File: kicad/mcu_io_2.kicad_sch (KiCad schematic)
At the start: 1 part, among them U5 MCXN947VDFT

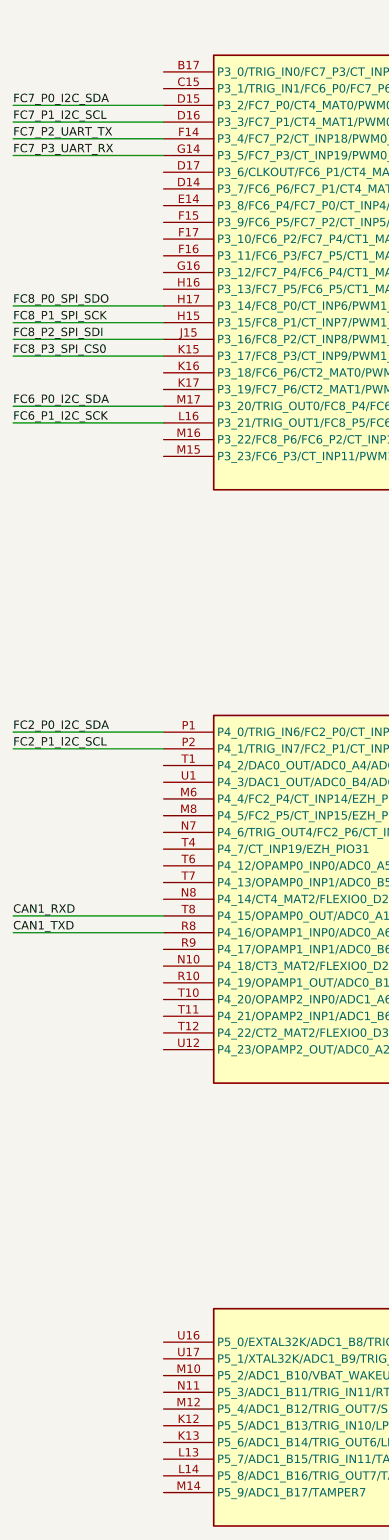
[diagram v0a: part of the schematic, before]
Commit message: Updated schematics and BOM.
- Finished power supply schematics
- Added power schematic around MCXN
- Assigned MCXN pins
- Created board-to-board schematic and assigned pins to DF40T board-to-board connector
- Added correct sensors, finished sensor schematic
- Updated parts in communication schematic
- Added all part numbers etc in parts parameters
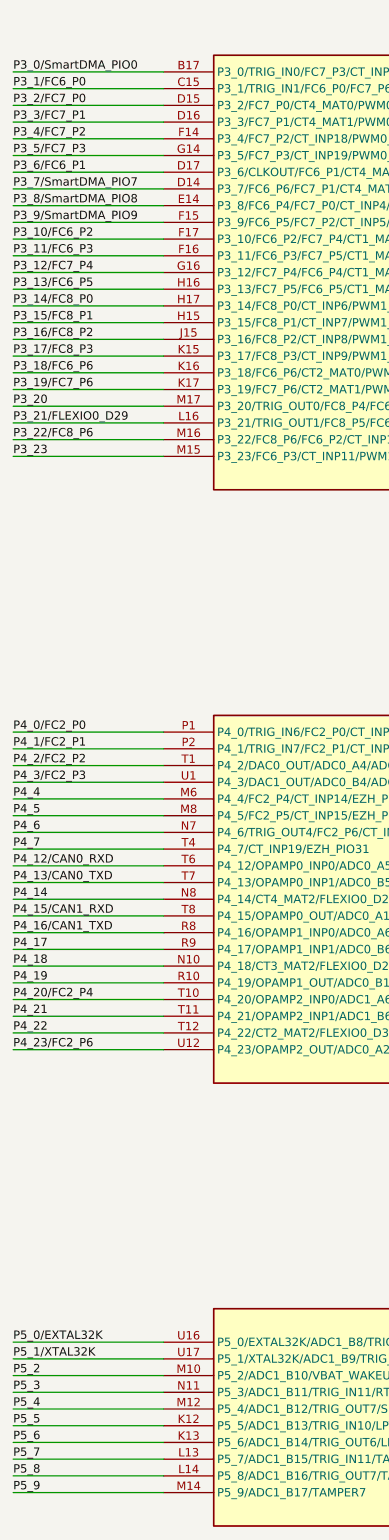
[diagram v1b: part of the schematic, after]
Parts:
- U5: MF (none) -> NXP USA Inc.; MFPN (none) -> MCXN947VDFT; Supplier (none) -> DigiKey; Supplier PN (none) -> 568-MCXN947VDFT-ND
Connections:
- net P4_4: now reaches U5.M6 (P4_4/FC2_P4/CT_INP14/EZH_PIO28/PLU_IN4/SINC0_MCLK4)
- net P4_5: now reaches U5.M8 (P4_5/FC2_P5/CT_INP15/EZH_PIO29/PLU_IN5/SINC0_MBIT4)
- net P4_18: now reaches U5.N10 (P4_18/CT3_MAT2/FLEXIO0_D26/PLU_OUT6)
- net P4_6: now reaches U5.N7 (P4_6/TRIG_OUT4/FC2_P6/CT_INP18/EZH_PIO30/PLU_CLK)
- net P4_14: now reaches U5.N8 (P4_14/CT4_MAT2/FLEXIO0_D22/PLU_OUT2)
- net P4_19: now reaches U5.R10 (P4_19/OPAMP1_OUT/ADC0_B1/CMP1_IN4P/TRIG_OUT5/CT3_MAT3/FLEXIO0_D27/PLU_OUT7/SINC0_MCLK_OUT1)
- net P4_17: now reaches U5.R9 (P4_17/OPAMP1_INP1/ADC0_B6/TRIG_IN9/FC2_P3/USB1_OTG_OC/CT3_MAT1/FLEXIO0_D25/PLU_OUT5/SINC0_MBIT1)
- net P4_2/FC2_P2: now reaches U5.T1 (P4_2/DAC0_OUT/ADC0_A4/ADC1_A4/CMP0_IN4N/CMP1_IN4N/CMP2_IN4N/TRIG_IN6/FC2_P2/CT_INP12/EZH_PIO26/PLU_IN2/SINC0_MBIT3)
- net P4_20/FC2_P4: now reaches U5.T10 (P4_20/OPAMP2_INP0/ADC1_A6/TRIG_IN8/FC2_P4/CT2_MAT0/FLEXIO0_D28/SINC0_MCLK2)
- net P4_21: now reaches U5.T11 (P4_21/OPAMP2_INP1/ADC1_B6/TRIG_IN9/FC2_P5/CT2_MAT1/FLEXIO0_D29/SINC0_MBIT2)
- net P4_22: now reaches U5.T12 (P4_22/CT2_MAT2/FLEXIO0_D30)
- net P4_7: now reaches U5.T4 (P4_7/CT_INP19/EZH_PIO31)
- net P4_12/CAN0_RXD: now reaches U5.T6 (P4_12/OPAMP0_INP0/ADC0_A5/ADC1_A5/USB0_VBUS_DET/FC2_P0/CT4_MAT0/FLEXIO0_D20/PLU_OUT0/SINC0_MCLK0/CAN0_RXD/MTR_START_BURNIN/WUU0_IN20)
- net P4_13/CAN0_TXD: now reaches U5.T7 (P4_13/OPAMP0_INP1/ADC0_B5/ADC1_B5/TRIG_IN8/FC2_P1/USB1_ID/CT4_MAT1/FLEXIO0_D21/PLU_OUT1/SINC0_MBIT0/CAN0_TXD)
- net P4_3/FC2_P3: now reaches U5.U1 (P4_3/DAC1_OUT/ADC0_B4/ADC1_B4/CMP0_IN5N/CMP1_IN5N/CMP2_IN5N/TRIG_IN7/FC2_P3/CT_INP13/EZH_PIO27/PLU_IN3/WUU0_IN19)
- net P4_23/FC2_P6: now reaches U5.U12 (P4_23/OPAMP2_OUT/ADC0_A2/ADC0_B2/ADC1_B3/CMP2_IN4P/TRIG_OUT5/FC2_P6/CT2_MAT3/FLEXIO0_D31/SINC0_MCLK_OUT2)
- net P3_0/SmartDMA_PIO0: now reaches U5.B17 (P3_0/TRIG_IN0/FC7_P3/CT_INP16/PWM0_A0/FLEXIO0_D8/EZH_PIO0/FLEXSPI0_A_SS0_b/PF_QSPI_CS0_DIS/TP_HWRITE/WUU0_IN22)
- net P3_1/FC6_P0: now reaches U5.C15 (P3_1/TRIG_IN1/FC6_P0/FC7_P6/CT_INP17/PWM0_B0/FLEXIO0_D9/EZH_PIO1/FLEXSPI0_A_SS1_b/PF_QSPI_CS1_DIS/FREQME_CLK_OUT0)
- net P3_7/SmartDMA_PIO7: now reaches U5.D14 (P3_7/FC6_P6/FC7_P1/CT4_MAT3/PWM0_B1/FLEXIO0_D15/EZH_PIO7/FLEXSPI0_A_SCLK/SIM0_VCCEN/SAI0_MCLK/PF_QSPI_SCKIN/TP_LOAD_EN)
- net P3_6/FC6_P1: now reaches U5.D17 (P3_6/CLKOUT/FC6_P1/CT4_MAT2/PWM0_A1/FLEXIO0_D14/EZH_PIO6/FLEXSPI0_A_DQS/SIM1_VCCEN/SAI1_MCLK/PF_QSPI_CS_n/FREQME_CLK_OUT1/ADC0_CONV_CLK)
- net P3_8/SmartDMA_PIO8: now reaches U5.E14 (P3_8/FC6_P4/FC7_P0/CT_INP4/PWM0_A2/FLEXIO0_D16/EZH_PIO8/FLEXSPI0_A_DATA0/SIM0_PD/SAI0_TX_BCLK/PF_QSPI_DATA0/TP_ADDR0/WUU0_IN23)
- net P3_9/SmartDMA_PIO9: now reaches U5.F15 (P3_9/FC6_P5/FC7_P2/CT_INP5/PWM0_B2/FLEXIO0_D17/EZH_PIO9/FLEXSPI0_A_DATA1/SIM0_RST/SAI0_TX_FS/PF_QSPI_DATA1/TP_ADDR1)
- net P3_11/FC6_P3: now reaches U5.F16 (P3_11/FC6_P3/FC7_P5/CT1_MAT1/PWM0_B3/FLEXIO0_D19/EZH_PIO11/FLEXSPI0_A_DATA3/SIM0_IO/SAI0_RXD0/PF_QSPI_DATA3/USB1_TSTI_TX_LS_EN/TP_ADDR3/WUU0_IN24)
- net P3_10/FC6_P2: now reaches U5.F17 (P3_10/FC6_P2/FC7_P4/CT1_MAT0/PWM0_A3/FLEXIO0_D18/EZH_PIO10/FLEXSPI0_A_DATA2/SIM0_CLK/SAI0_TXD0/PF_QSPI_DATA2/USB1_TSTI_TX_HS_MODE/TP_ADDR2)
- net P3_12/FC7_P4: now reaches U5.G16 (P3_12/FC7_P4/FC6_P4/CT1_MAT2/PWM1_A0/FLEXIO0_D20/EZH_PIO12/FLEXSPI0_A_DATA4/SAI0_RXD1/USB1_TSTI_TX_ENAB/ADC0_CONV_DATA0)
- net P3_13/FC6_P5: now reaches U5.H16 (P3_13/FC7_P5/FC6_P5/CT1_MAT3/PWM1_B0/FLEXIO0_D21/EZH_PIO13/FLEXSPI0_A_DATA5/SAI0_TXD1/PF_SPI_CS0_n/USB1_TSTI_TX_HIZ/ADC0_CONV_DATA1)
- net P3_18/FC6_P6: now reaches U5.K16 (P3_18/FC6_P6/CT2_MAT0/PWM1_X0/FLEXIO0_D26/EZH_PIO18/SAI1_RX_BCLK)
- net P3_19/FC7_P6: now reaches U5.K17 (P3_19/FC7_P6/CT2_MAT1/PWM1_X1/FLEXIO0_D27/EZH_PIO19/SAI1_RX_FS)
- net P3_23: now reaches U5.M15 (P3_23/FC6_P3/CT_INP11/PWM1_X3/FLEXIO0_D31/EZH_PIO23/SAI1_TXD1)
- net P3_22/FC8_P6: now reaches U5.M16 (P3_22/FC8_P6/FC6_P2/CT_INP10/PWM1_X2/FLEXIO0_D30/EZH_PIO22/SIM0_VCCEN/SAI1_RXD1)
- net P5_5: now reaches U5.K12 (P5_5/ADC1_B13/TRIG_IN10/LPTMR0_ALT2/TAMPER3)
- net P5_6: now reaches U5.K13 (P5_6/ADC1_B14/TRIG_OUT6/LPTMR1_ALT2/TAMPER4)
- net P5_7: now reaches U5.L13 (P5_7/ADC1_B15/TRIG_IN11/TAMPER5)
- net P5_8: now reaches U5.L14 (P5_8/ADC1_B16/TRIG_OUT7/TAMPER6)
- net P5_2: now reaches U5.M10 (P5_2/ADC1_B10/VBAT_WAKEUP_b/SPC_LPREQ/TAMPER0)
- net P5_4: now reaches U5.M12 (P5_4/ADC1_B12/TRIG_OUT7/SPC_LPREQ/TAMPER2)
- net P5_9: now reaches U5.M14 (P5_9/ADC1_B17/TAMPER7)
- net P5_3: now reaches U5.N11 (P5_3/ADC1_B11/TRIG_IN11/RTC_CLKOUT/TAMPER1)
- net P5_0/EXTAL32K: now reaches U5.U16 (P5_0/EXTAL32K/ADC1_B8/TRIG_IN10/LPTMR0_ALT2)
- net P5_1/XTAL32K: now reaches U5.U17 (P5_1/XTAL32K/ADC1_B9/TRIG_OUT6/LPTMR1_ALT2)
- net CAN1_RXD renamed P4_15/CAN1_RXD
- net CAN1_TXD renamed P4_16/CAN1_TXD
- net FC2_P0_I2C_SDA renamed P4_0/FC2_P0
- net FC2_P1_I2C_SCL renamed P4_1/FC2_P1
- net FC6_P0_I2C_SDA renamed P3_20
- net FC6_P1_I2C_SCK renamed P3_21/FLEXIO0_D29
- net FC7_P0_I2C_SDA renamed P3_2/FC7_P0
- net FC7_P1_I2C_SCL renamed P3_3/FC7_P1
- net FC7_P2_UART_TX renamed P3_4/FC7_P2
- net FC7_P3_UART_RX renamed P3_5/FC7_P3
- net FC8_P0_SPI_SDO renamed P3_14/FC8_P0
- net FC8_P1_SPI_SCK renamed P3_15/FC8_P1
- net FC8_P2_SPI_SDI renamed P3_16/FC8_P2
- net FC8_P3_SPI_CS0 renamed P3_17/FC8_P3

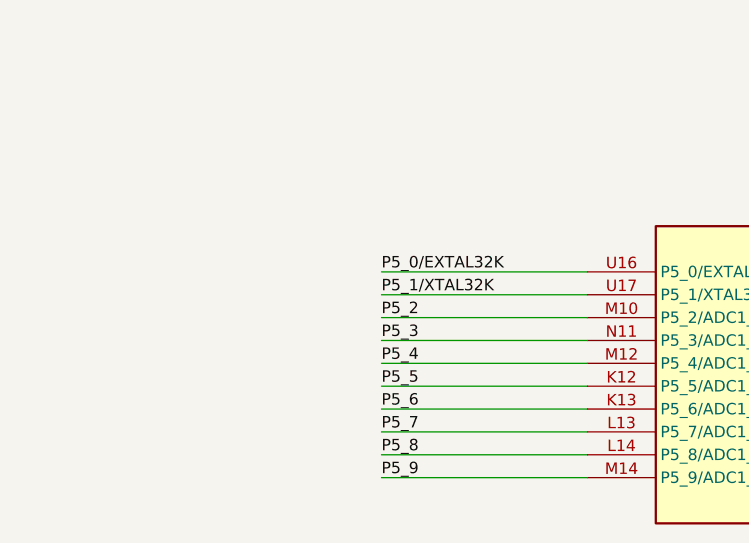
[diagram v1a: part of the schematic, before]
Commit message: Finished schematic design for first review
Finished schematic design for first review.
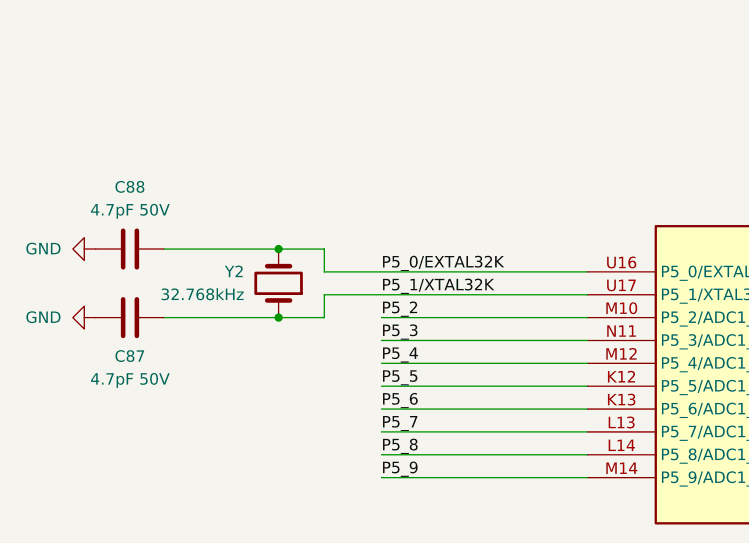
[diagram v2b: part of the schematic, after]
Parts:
- added C87, C88: 4.7pF 50V, Capacitor_SMD:C_0402_1005Metric, symbol Device:C
- added Y2: 32.768kHz, Crystal:Crystal_SMD_3215-2Pin_3.2x1.5mm, symbol Device:Crystal
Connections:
- net P5_0/EXTAL32K: now also C88.1, Y2.2
- net P5_1/XTAL32K: now also C87.1, Y2.1
- new net GND: C87.2, C88.2

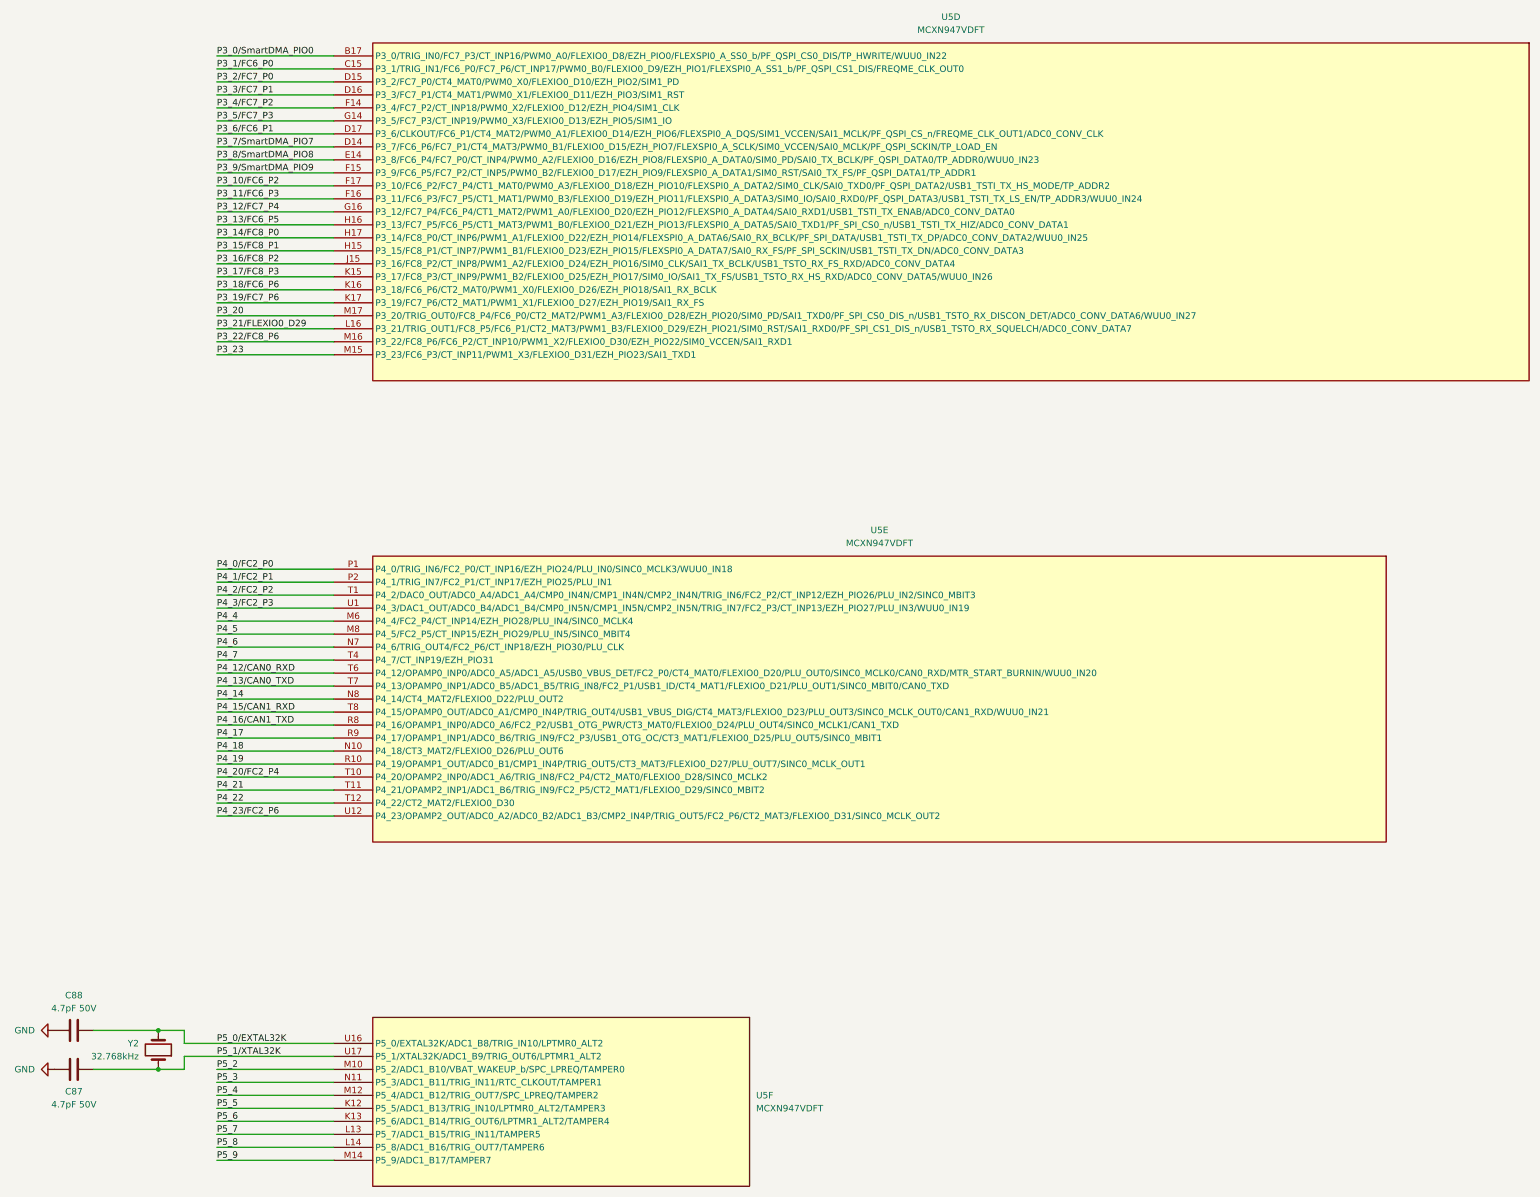
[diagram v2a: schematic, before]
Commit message: Updated schematic and started on layout
- Implemented schematic changes after feedback:
	- BMM350 VDD is 1.8V
	- Replaced net labels with global labels for page references
	- Added 1uF cap to SK9822-EC20
- Added rev-RMII configuration for TJA1103 and DNP resistor to put it in slave mode
- Added TJA1103 PHY address info
- Changed decoupling caps for MCXN to smallest possible packages
- Added traces and vias at MCXN according to guidelines
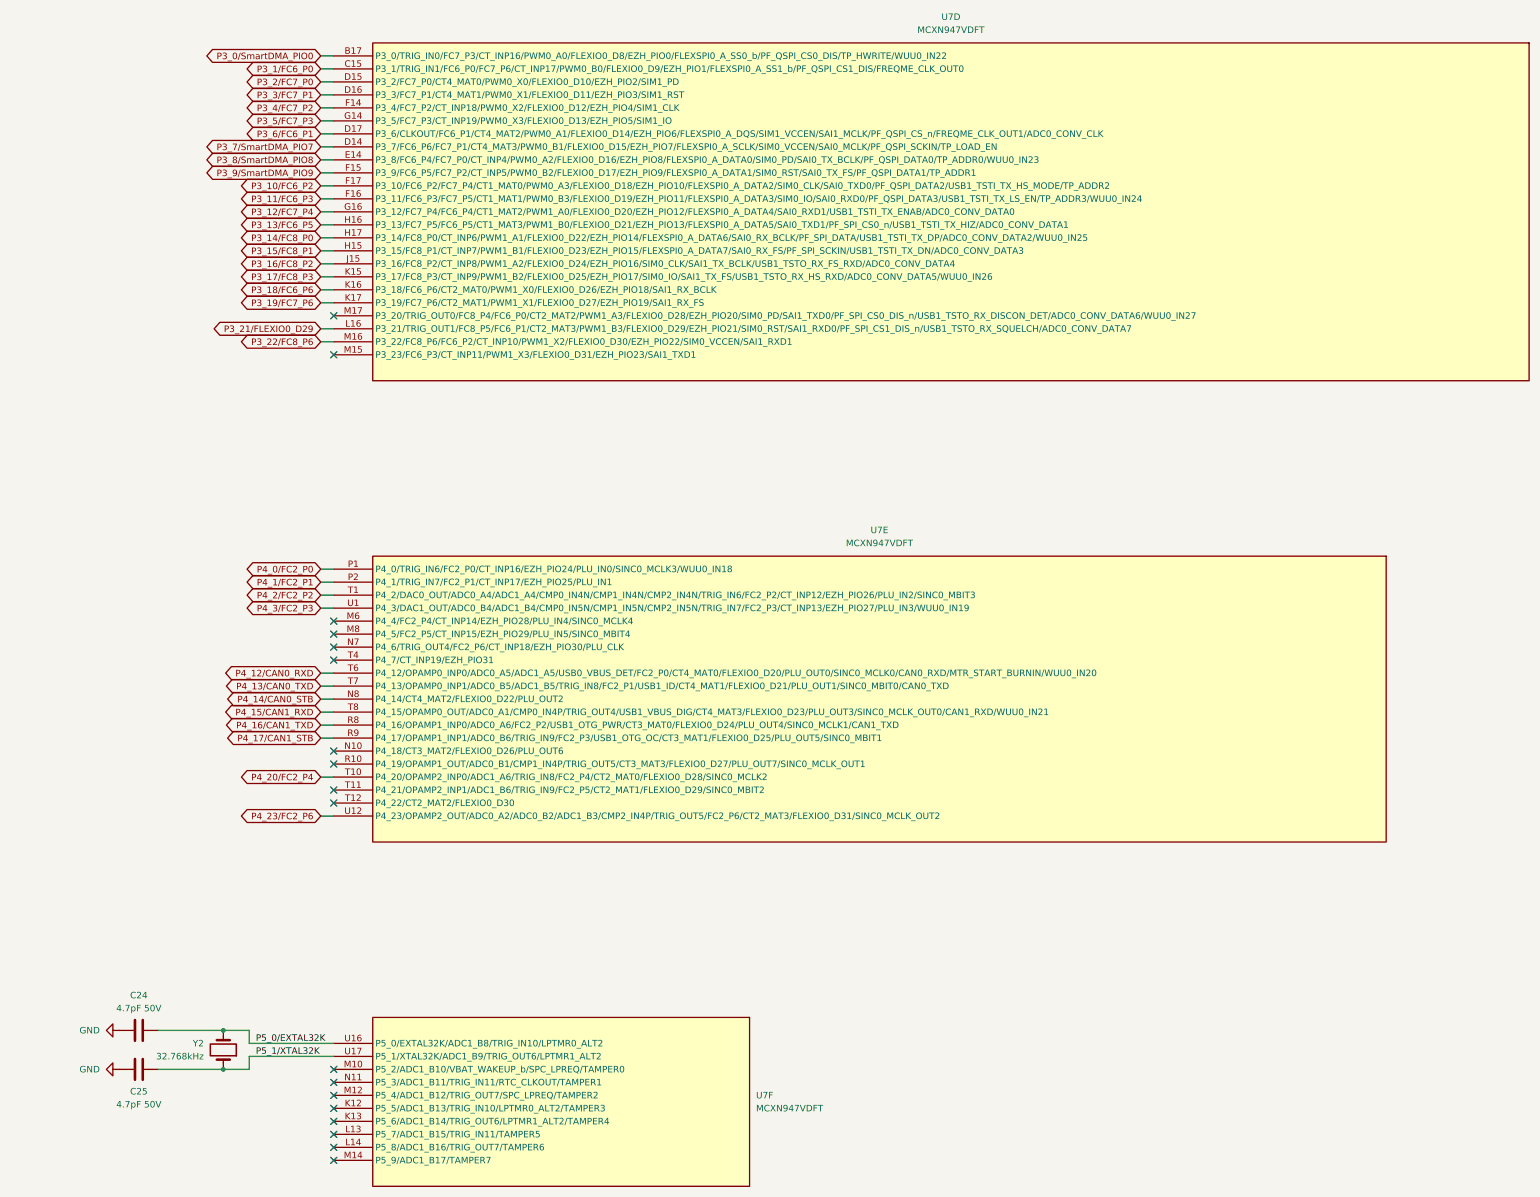
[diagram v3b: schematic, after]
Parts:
- renumbered C88 to C24, C87 to C25, U5 to U7
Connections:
- net P3_20: no longer names the net of U7.M17 (P3_20/TRIG_OUT0/FC8_P4/FC6_P0/CT2_MAT2/PWM1_A3/FLEXIO0_D28/EZH_PIO20/SIM0_PD/SAI1_TXD0/PF_SPI_CS0_DIS_n/USB1_TSTO_RX_DISCON_DET/ADC0_CONV_DATA6/WUU0_IN27)
- net P3_23: no longer names the net of U7.M15 (P3_23/FC6_P3/CT_INP11/PWM1_X3/FLEXIO0_D31/EZH_PIO23/SAI1_TXD1)
- net P4_14 renamed P4_14/CAN0_STB
- net P4_17 renamed P4_17/CAN1_STB
- net P4_18: no longer names the net of U7.N10 (P4_18/CT3_MAT2/FLEXIO0_D26/PLU_OUT6)
- net P4_19: no longer names the net of U7.R10 (P4_19/OPAMP1_OUT/ADC0_B1/CMP1_IN4P/TRIG_OUT5/CT3_MAT3/FLEXIO0_D27/PLU_OUT7/SINC0_MCLK_OUT1)
- net P4_21: no longer names the net of U7.T11 (P4_21/OPAMP2_INP1/ADC1_B6/TRIG_IN9/FC2_P5/CT2_MAT1/FLEXIO0_D29/SINC0_MBIT2)
- net P4_22: no longer names the net of U7.T12 (P4_22/CT2_MAT2/FLEXIO0_D30)
- net P4_4: no longer names the net of U7.M6 (P4_4/FC2_P4/CT_INP14/EZH_PIO28/PLU_IN4/SINC0_MCLK4)
- net P4_5: no longer names the net of U7.M8 (P4_5/FC2_P5/CT_INP15/EZH_PIO29/PLU_IN5/SINC0_MBIT4)
- net P4_6: no longer names the net of U7.N7 (P4_6/TRIG_OUT4/FC2_P6/CT_INP18/EZH_PIO30/PLU_CLK)
- net P4_7: no longer names the net of U7.T4 (P4_7/CT_INP19/EZH_PIO31)
- net P5_2: no longer names the net of U7.M10 (P5_2/ADC1_B10/VBAT_WAKEUP_b/SPC_LPREQ/TAMPER0)
- net P5_3: no longer names the net of U7.N11 (P5_3/ADC1_B11/TRIG_IN11/RTC_CLKOUT/TAMPER1)
- net P5_4: no longer names the net of U7.M12 (P5_4/ADC1_B12/TRIG_OUT7/SPC_LPREQ/TAMPER2)
- net P5_5: no longer names the net of U7.K12 (P5_5/ADC1_B13/TRIG_IN10/LPTMR0_ALT2/TAMPER3)
- net P5_6: no longer names the net of U7.K13 (P5_6/ADC1_B14/TRIG_OUT6/LPTMR1_ALT2/TAMPER4)
- net P5_7: no longer names the net of U7.L13 (P5_7/ADC1_B15/TRIG_IN11/TAMPER5)
- net P5_8: no longer names the net of U7.L14 (P5_8/ADC1_B16/TRIG_OUT7/TAMPER6)
- net P5_9: no longer names the net of U7.M14 (P5_9/ADC1_B17/TAMPER7)
- no-connect marks 0 -> 18
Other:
- moved on the sheet: C24, C25, Y2
